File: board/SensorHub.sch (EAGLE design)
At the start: 32 parts, among them IC1 PIC12F629P, X1 RJ45-6LC21-B, X2 RJ45-6LC21-B, X3 RJ45-6LC21-B, X4 RJ45-6LC21-B, X5 RJ45-6LC21-B, X6 RJ45-6LC21-B, X7 RJ45-6LC21-B, X8 RJ45-6LC21-B, X9 22-23-2081

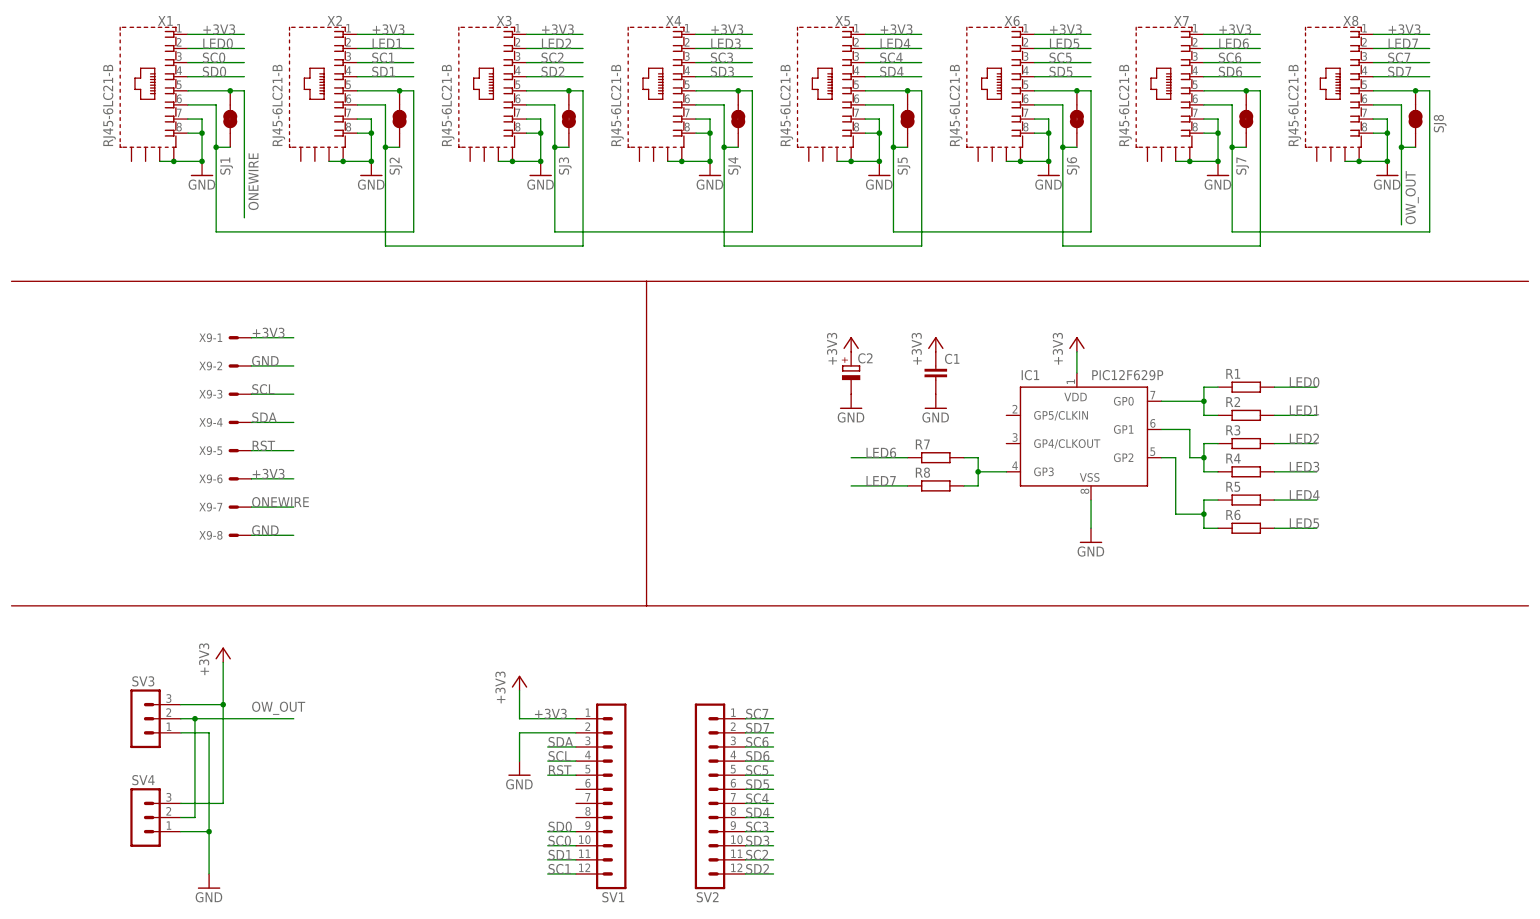
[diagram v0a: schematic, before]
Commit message: sensor hub with power lines only
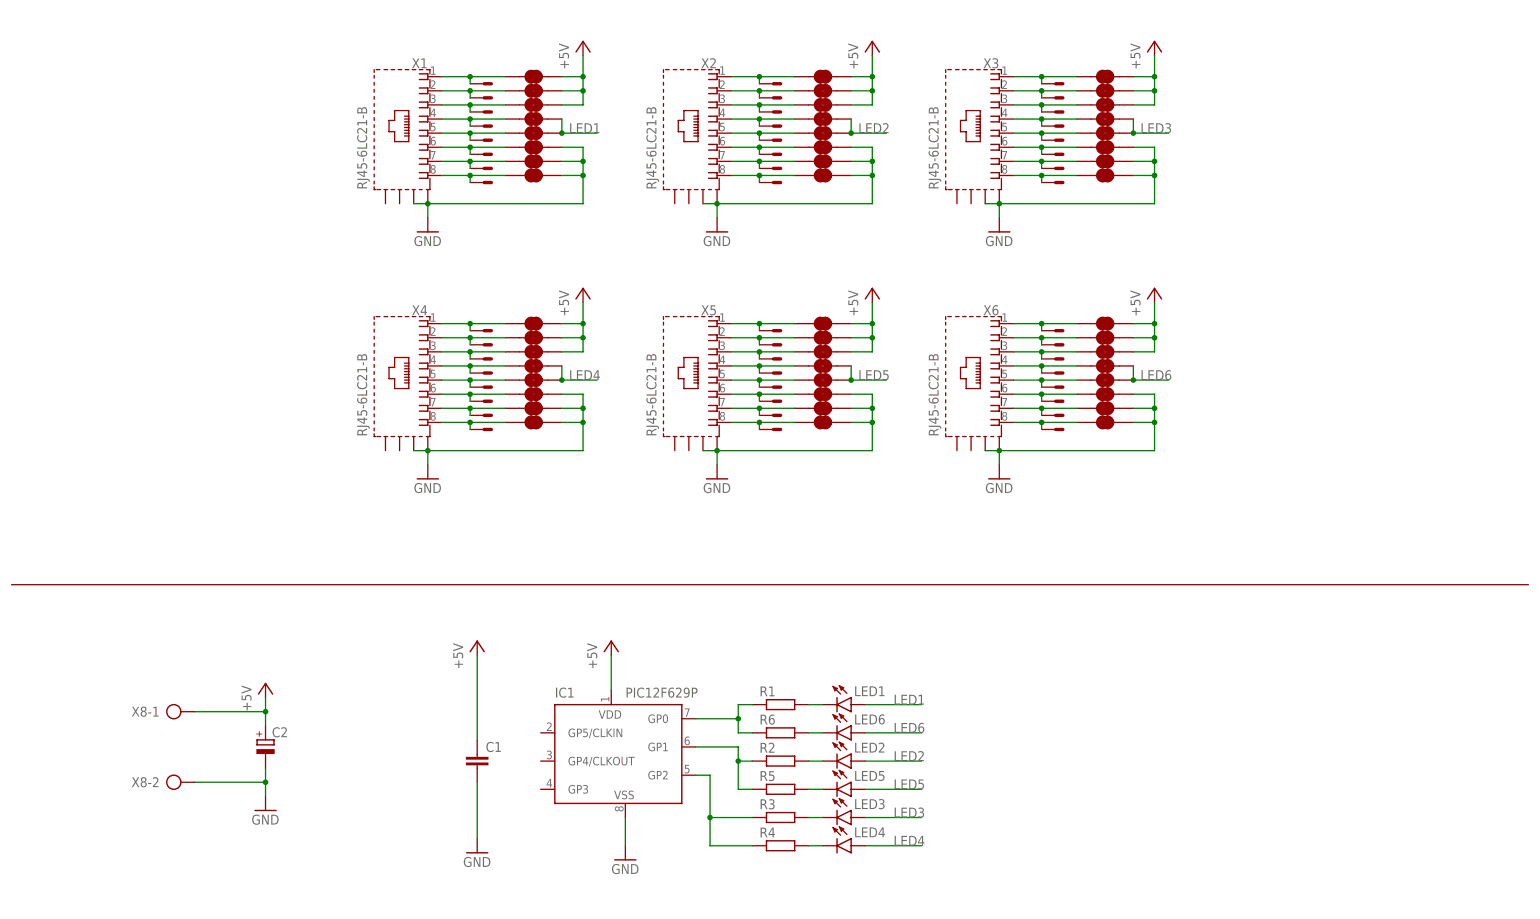
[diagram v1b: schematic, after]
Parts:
- removed R7, R8: (no value), rcl:R-EU_0207/10
- removed SJ1, SJ2, SJ3, SJ4, SJ5, SJ6, SJ7, SJ8: JUMPER-SMT_2_NC_TRACE_SILK, SparkFun-Jumpers:JUMPER-SMT_2_NC_TRACE_SILK
- removed SV1, SV2: (no value), con-lstb:MA12-1
- removed SV3, SV4: (no value), con-lstb:MA03-1
- removed X7: RJ45-6LC21-B, con-tycoelectronics:RJ45-6LC21-B
- removed X9: 22-23-2081, con-molex:22-23-2081
- added JP1, JP10, JP11, JP12, JP13, JP14, JP15, JP16, JP17, JP18, JP19, JP2, JP20, JP21, JP22, JP23, JP24, JP25, JP26, JP27, JP28, JP29, JP3, JP30, JP31, JP32, JP33, JP34, JP35, JP36, JP37, JP38, JP39, JP4, JP40, JP41, JP42, JP43, JP44, JP45, JP46, JP47, JP48, JP5, JP6, JP7, JP8, JP9: JUMPER-SMT_2_NC_TRACE_SILK, SparkFun-Jumpers:JUMPER-SMT_2_NC_TRACE_SILK
- added LED1, LED2, LED3, LED4, LED5, LED6: TLLR4400, led:TLLR4400
- added X1.1, X1.2, X1.3, X1.4, X1.5, X1.6: 22-23-2081, con-molex:22-23-2081
- X8: value RJ45-6LC21-B -> (none); device con-tycoelectronics:RJ45-6LC21-B -> con-ptr500:AK500/2
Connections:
- removed net +3V3: C1.1, C2.+, IC1.VDD, SV1.1, SV3.3, SV4.3, X1.1, X2.1, X3.1, X4.1, X5.1, X6.1, X7.1, X8.1, X9-1.S, X9-6.S
- removed net LED0: R1.2, X1.2
- removed net LED7: R8.1, X8.2
- removed net ONEWIRE: SJ1.2, X1.5, X9-7.S
- removed net OW_OUT: SJ8.1, SV3.2, SV4.2, X8.6
- removed net RST: SV1.5, X9-5.S
- removed net SC0: SV1.10, X1.3
- removed net SC1: SV1.12, X2.3
- removed net SC2: SV2.11, X3.3
- removed net SC3: SV2.9, X4.3
- removed net SC4: SV2.7, X5.3
- removed net SC5: SV2.5, X6.3
- removed net SC6: SV2.3, X7.3
- removed net SC7: SV2.1, X8.3
- removed net SCL: SV1.4, X9-3.S
- removed net SD0: SV1.9, X1.4
- removed net SD1: SV1.11, X2.4
- removed net SD2: SV2.12, X3.4
- removed net SD3: SV2.10, X4.4
- removed net SD4: SV2.8, X5.4
- removed net SD5: SV2.6, X6.4
- removed net SD6: SV2.4, X7.4
- removed net SD7: SV2.2, X8.4
- removed net SDA: SV1.3, X9-4.S
- new net +5V: C1.1, C2.+, IC1.VDD, JP1.2, JP10.2, JP11.2, JP17.2, JP18.2, JP19.2, JP2.2, JP25.2, JP26.2, JP27.2, JP3.2, JP33.2, JP34.2, JP35.2, JP41.2, JP42.2, JP43.2, JP9.2, X8-1.KL
- new net N$1: JP1.1, X1.1, X1.1-1.S
- new net N$11: LED1.C, R1.2
- new net N$13: LED3.C, R3.2
- new net N$15: LED5.C, R5.2
- new net N$16: LED4.C, R4.2
- new net N$17: JP10.1, X1.2-2.S, X2.2
- new net N$19: JP12.1, X1.2-4.S, X2.4
- new net N$2: JP2.1, X1.1-2.S, X1.2
- new net N$23: JP14.1, X1.2-6.S, X2.6
- new net N$24: JP15.1, X1.2-7.S, X2.7
- new net N$25: JP16.1, X1.2-8.S, X2.8
- new net N$26: JP17.1, X1.3-1.S, X3.1
- new net N$27: JP18.1, X1.3-2.S, X3.2
- new net N$28: JP19.1, X1.3-3.S, X3.3
- new net N$29: JP20.1, X1.3-4.S, X3.4
- new net N$30: JP21.1, X1.3-5.S, X3.5
- new net N$31: JP22.1, X1.3-6.S, X3.6
- new net N$32: JP23.1, X1.3-7.S, X3.7
- new net N$33: JP24.1, X1.3-8.S, X3.8
- new net N$34: JP25.1, X1.4-1.S, X4.1
- new net N$35: JP26.1, X1.4-2.S, X4.2
- new net N$36: JP27.1, X1.4-3.S, X4.3
- new net N$37: JP28.1, X1.4-4.S, X4.4
- new net N$38: JP29.1, X1.4-5.S, X4.5
- new net N$39: JP30.1, X1.4-6.S, X4.6
- new net N$4: JP4.1, X1.1-4.S, X1.4
- new net N$40: JP31.1, X1.4-7.S, X4.7
- new net N$41: JP32.1, X1.4-8.S, X4.8
- new net N$42: JP33.1, X1.5-1.S, X5.1
- new net N$43: JP34.1, X1.5-2.S, X5.2
- new net N$44: JP35.1, X1.5-3.S, X5.3
- new net N$45: JP36.1, X1.5-4.S, X5.4
- new net N$46: JP37.1, X1.5-5.S, X5.5
- new net N$47: JP38.1, X1.5-6.S, X5.6
- new net N$48: JP39.1, X1.5-7.S, X5.7
- new net N$49: JP40.1, X1.5-8.S, X5.8
- new net N$50: JP41.1, X1.6-1.S, X6.1
- new net N$51: JP42.1, X1.6-2.S, X6.2
- new net N$52: JP43.1, X1.6-3.S, X6.3
- new net N$53: JP44.1, X1.6-4.S, X6.4
- new net N$54: JP45.1, X1.6-5.S, X6.5
- new net N$55: JP46.1, X1.6-6.S, X6.6
- new net N$56: JP47.1, X1.6-7.S, X6.7
- new net N$57: JP48.1, X1.6-8.S, X6.8
- new net N$6: JP6.1, X1.1-6.S, X1.6
- new net N$9: JP9.1, X1.2-1.S, X2.1
- net GND: now also JP14.2, JP15.2, JP16.2, JP22.2, JP23.2, JP24.2, JP30.2, JP31.2, JP32.2, JP38.2, JP39.2, JP40.2, JP46.2, JP47.2, JP48.2, JP6.2, JP7.2, JP8.2, X8-2.KL; no longer SV1.2, SV3.1, SV4.1, X1.7, X1.8, X2.7, X2.8, X3.7, X3.8, X4.7, X4.8, X5.7, X5.8, X6.7, X6.8, X7.7, X7.8, X7.S@1, X7.S@2, X8.7, X8.8, X8.S@1, X8.S@2, X9-2.S, X9-8.S
- net LED1: now also JP4.2, JP5.2, LED1.A; no longer R2.2, X2.2
- net LED2: now also JP12.2, JP13.2, LED2.A; no longer R3.2, X3.2
- net LED3: now also JP20.2, JP21.2, LED3.A; no longer R4.2, X4.2
- net LED4: now also JP28.2, JP29.2, LED4.A; no longer R5.2, X5.2
- net LED5: now also JP36.2, JP37.2, LED5.A; no longer R6.2, X6.2
- net LED6: now also JP44.2, JP45.2, LED6.A; no longer R7.1, X7.2
- net N$10: now also IC1.GP1, R2.1, R5.1; no longer SJ6.1, SJ7.2, X6.6, X7.5
- net N$12: now also LED2.C, R2.2; no longer SJ7.1, SJ8.2, X7.6, X8.5
- net N$14: now also LED6.C, R6.2; no longer SJ2.1, SJ3.2, X2.6, X3.5
- net N$18: now also JP11.1, X1.2-3.S, X2.3; no longer IC1.GP3, R7.2, R8.2
- net N$20: now also R6.1; no longer R2.1
- net N$21: now also JP13.1, X1.2-5.S, X2.5; no longer IC1.GP1, R3.1, R4.1
- net N$22: now also R3.1, R4.1; no longer R5.1, R6.1
- net N$3: now also JP3.1, X1.1-3.S, X1.3; no longer SJ3.1, SJ4.2, X3.6, X4.5
- net N$5: now also JP5.1, X1.1-5.S, X1.5; no longer SJ1.1, SJ2.2, X1.6, X2.5
- net N$7: now also JP7.1, X1.1-7.S, X1.7; no longer SJ4.1, SJ5.2, X4.6, X5.5
- net N$8: now also JP8.1, X1.1-8.S, X1.8; no longer SJ5.1, SJ6.2, X5.6, X6.5
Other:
- moved on the sheet: C1, C2, IC1, R1, R2, R3, R4, R5, R6, X1, X2, X3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
